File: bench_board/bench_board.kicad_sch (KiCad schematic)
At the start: 42 parts, among them J1 BATT_2S, J2 BOOT0_JUMPER, J3 USB-C, J4 CRSF_UART, J5 DSHOT_M1-M4, J6 SWD, U1 STM32F405RGT6, U2 TPS563201, U4 MPU-6000, U5 USBLC6-2SC6, Y1 8MHz

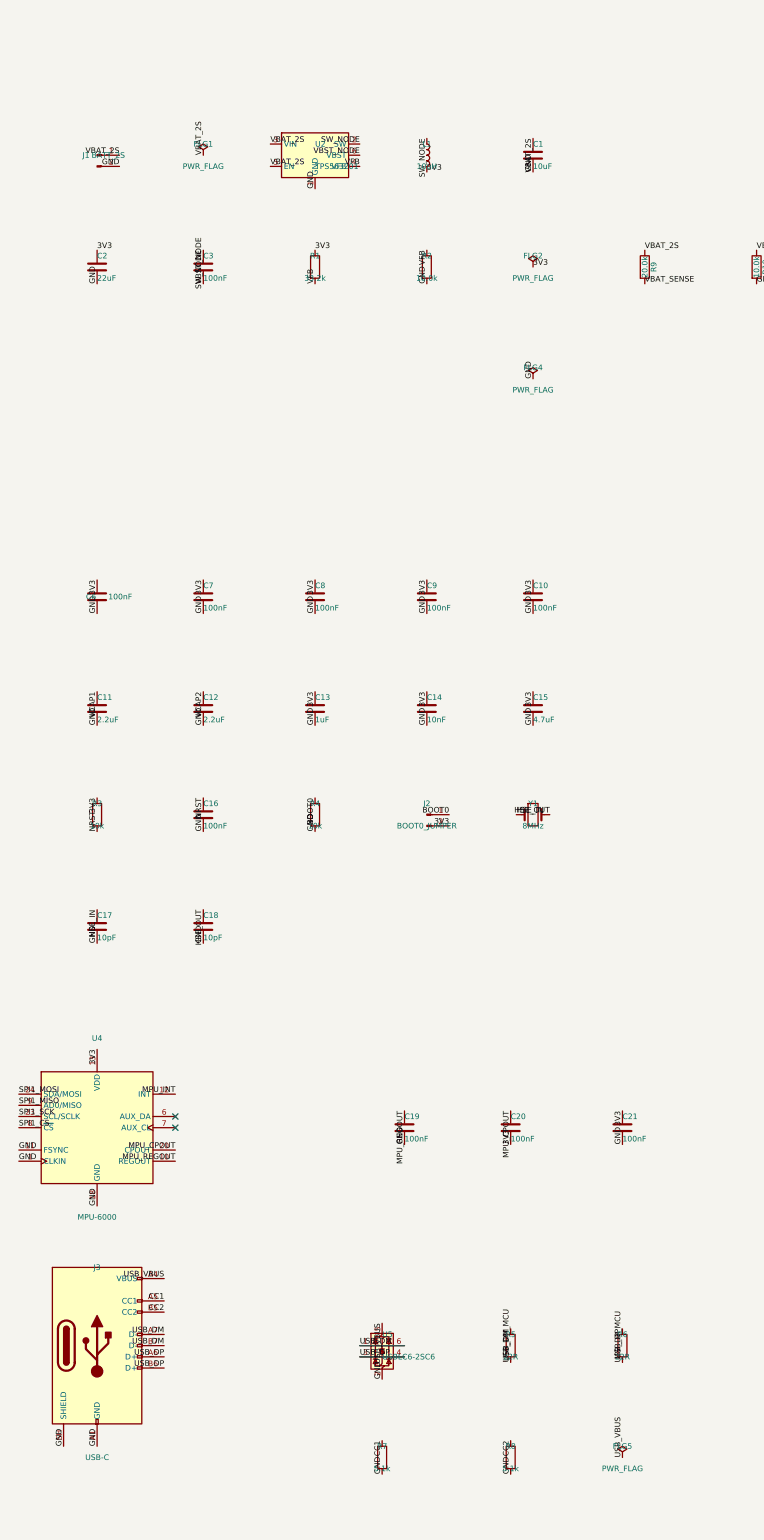
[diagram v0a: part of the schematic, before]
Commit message: Resolve outstanding schematic WIP: fix stale 2S values, add missing compensation network, verify AC loop stability
Item 1 review found the WIP wasn't just "uncommitted," it was incomplete
and partly wrong -- read the actual diff before trusting it:

- R1 was still the old 2S value (33.2k) despite the 4S doc already
  deriving 31.6k. Vout would have been 3.456V, not 3.3V. Fixed.
- R9/R10 (battery-sense divider) were still 2S values (20.0k/10.0k,
  divide-by-3.0). Even the documented 4S-era fix (49.9k) doesn't have
  ADC headroom at true 6S peak (25.2V -> 4.2V on a 3.3V pin). Recomputed
  for real 6S safety: R9=75.0k (8.5x ratio, 2.965V at 6S peak). Firmware
  updated to match (see drone-firmware commit cc91462).
- J1 was never renamed from BATT_2S to BATT_4S.
- U2 had no footprint assigned. Assigned the correct HSOIC-8/PowerPAD
  package per TI's own datasheet (fetched and text-extracted this batch).
- COMP/SS pins were wired to nothing -- no compensation network or
  soft-start cap existed at all. Placed real components (R11/C23
  compensation, C24 soft-start) sized from TI's own datasheet equations,
  then verified with a real AC loop-gain SPICE run (item 3): ~44kHz
  crossover, no instability at 4S or 6S, with an honest caveat about the
  average model's idealized phase response (see the SPICE doc's new §6).

Item 2: C1 bumped to a real 35V rating (was "≥25V" -- zero margin at true
25.2V 6S peak).

ERC: 0 errors, 0 warnings (was 2 warnings on the original WIP).

PCB sync/DRC not attempted -- separate, not-yet-done work, unchanged from
the prior 158-violation state.
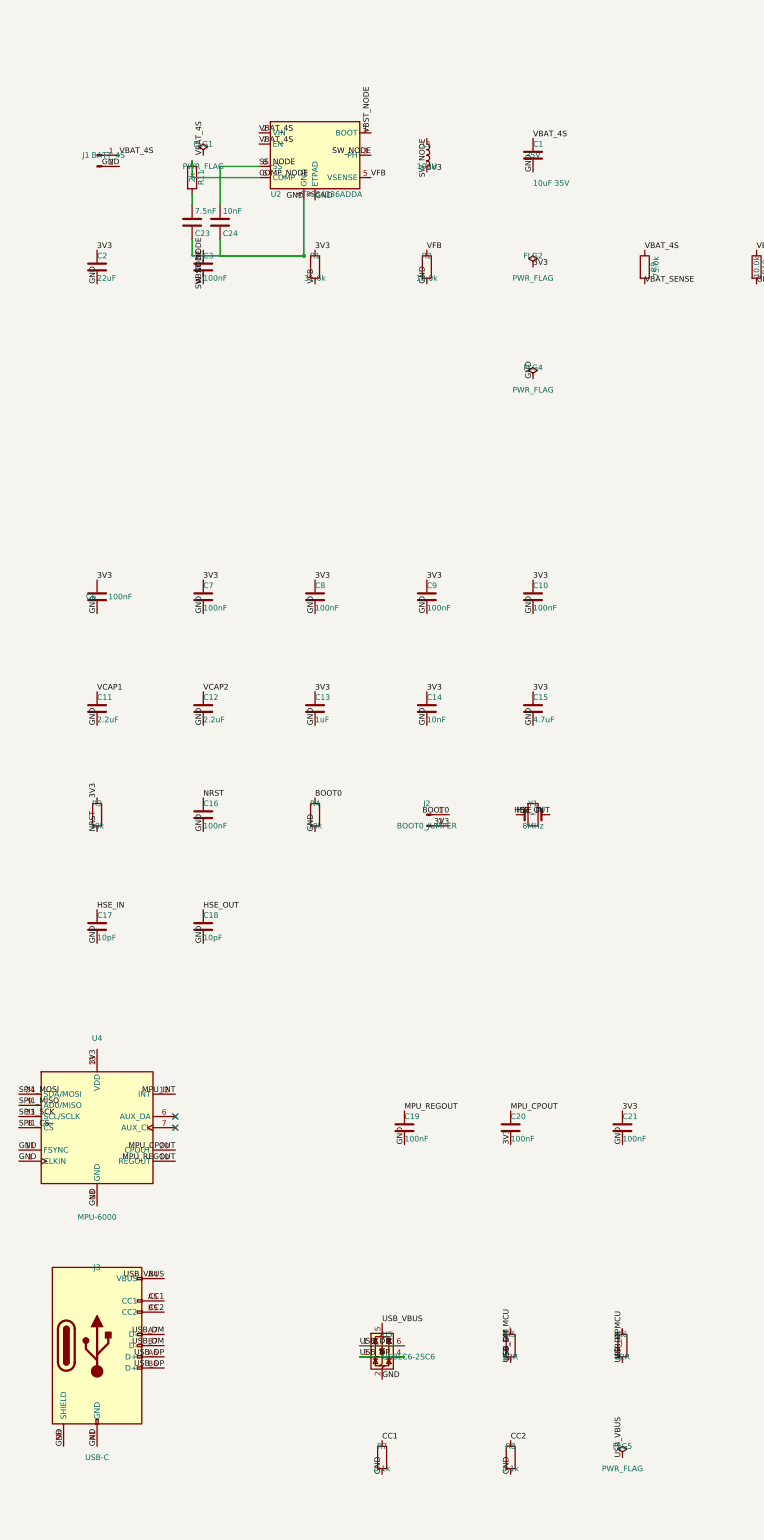
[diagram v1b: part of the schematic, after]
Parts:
- removed U2: TPS563201, Package_TO_SOT_SMD:SOT-23-6, symbol Regulator_Switching:TPS563201
- added C23: 7.5nF, Capacitor_SMD:C_0402_1005Metric, symbol Device:C
- added C24: 10nF, Capacitor_SMD:C_0402_1005Metric, symbol Device:C
- added R11: 2k, Resistor_SMD:R_0402_1005Metric, symbol Device:R
- added U2: TPS54336ADDA, Package_SO:SOIC-8-1EP_3.9x4.9mm_P1.27mm_EP2.41x3.81mm, symbol Regulator_Switching:TPS54336ADDA
- C1: value 10uF -> 10uF 35V; Voltage (none) -> 35V
- J1: value BATT_2S -> BATT_4S
- R1: value 33.2k -> 31.6k
- R9: value 20.0k -> 75.0k
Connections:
- net GND: now also C23.2, C24.2, U2.4 (GND), U2.9 (ETPAD)
- net SW_NODE: now also U2.3 (PH)
- net VBST_NODE: now also U2.1 (BOOT)
- net VFB: now also U2.5 (VSENSE)
- net VBAT_2S renamed VBAT_4S
- net VBAT_4S: now also U2.2 (VIN), U2.7 (EN)
- new net: C23.1, R11.2
- new net COMP_NODE: R11.1, U2.6 (COMP)
- new net SS_NODE: C24.1, U2.8 (SS)
